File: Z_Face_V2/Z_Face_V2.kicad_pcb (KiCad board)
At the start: 4 copper layers, 100 x 100 mm, 24 parts, among them J1 CON-5040500591, J4 Conn_01x01, J5 Conn_01x01, J6 Conn_01x01, J7 Conn_01x01, U1 VEML7700, U2 DRV2605LDGS, U3 MCP9808_DFN

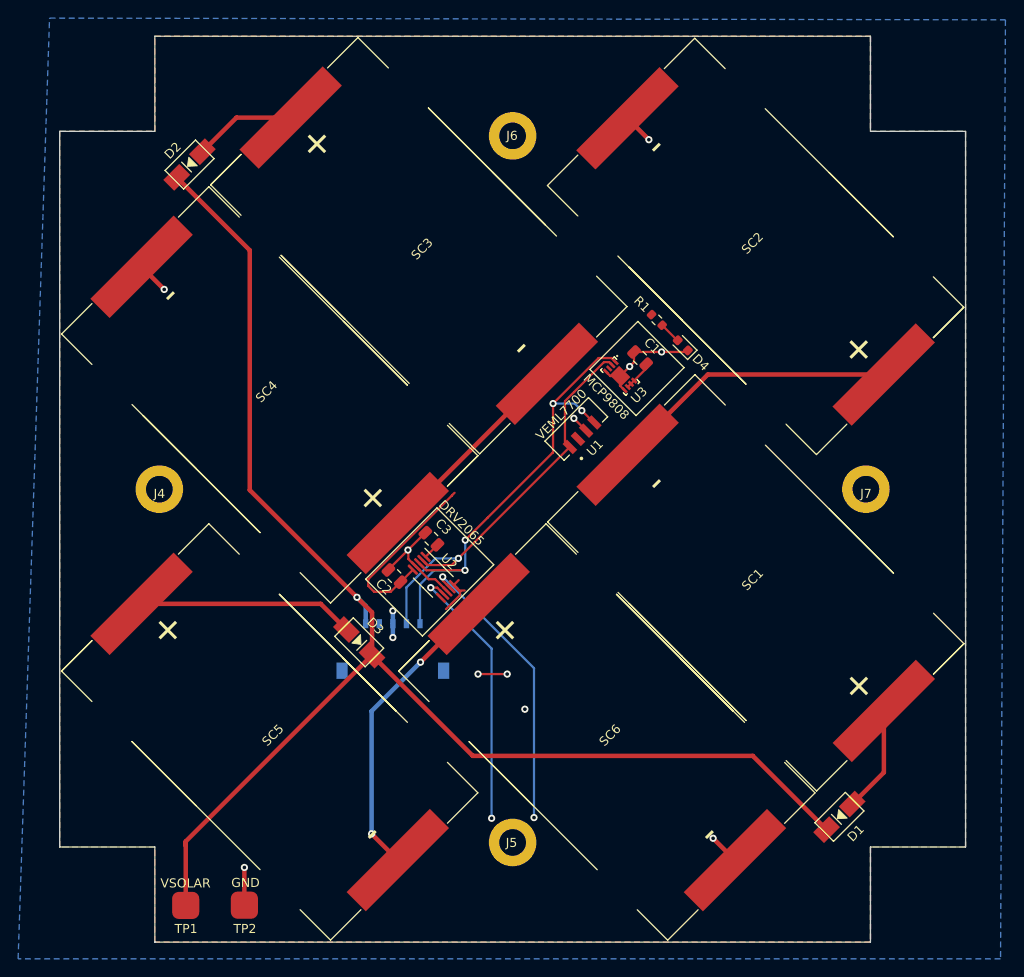
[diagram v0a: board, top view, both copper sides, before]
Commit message: Added 3-layer coil
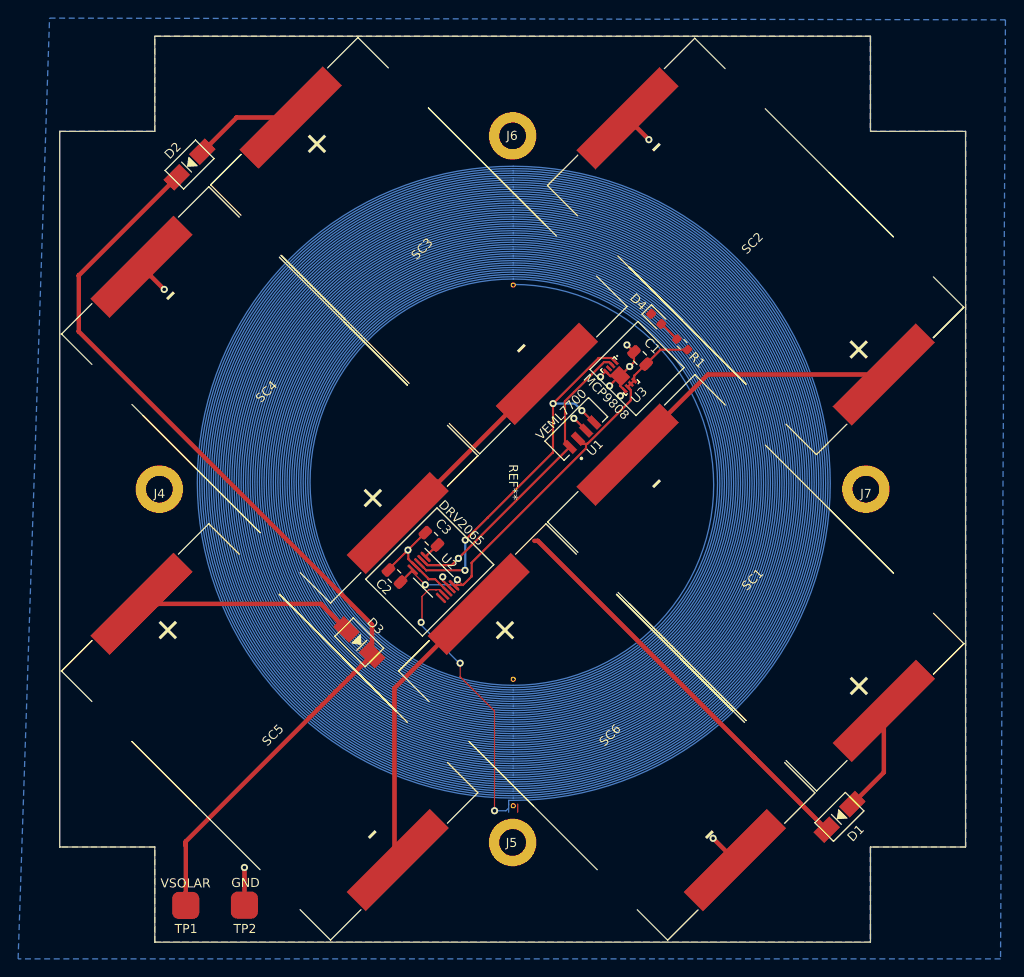
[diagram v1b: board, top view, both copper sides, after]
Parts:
- removed J1: CON-5040500591, SolarPanelBoards:CON_5040500591
- added REF**: 3Layer50Turn, dfsdf, F.Cu at (149.6, 84.2)
- moved D4 4.13 mm to (165.4, 66.2), turned to -45 degrees
- moved R1 3.89 mm to (168.2, 69.0), turned to 135 degrees
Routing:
- net Net-(U2-OUT+): track 10367.6 -> 47.9 mm, vias 5 -> 4
- net +3V3: track 32.6 -> 50.1 mm
- net SCL: track 44.8 -> 33.7 mm
- net SDA: track 52.3 -> 42.4 mm
- net VSOLAR: track 159.6 -> 152.9 mm, vias 1 -> 0
- net GND: track 45.0 -> 39.8 mm, vias 10 -> 11
- net Net-(SC5--): track 34.4 -> 32.3 mm, vias 2 -> 0
- added copper zone on F.Cu, net GND
- removed copper zone on F.Cu, net +3V3
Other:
- board text added: "PROVES BOTTOM CAP: V3 1U KIT"
- board text removed: "ADC I2C: JP1 Open (Defeult): 0x48 JP1 Solder Jumped: 0x49"
- board text removed: "ADC: ADS1015"
- board text removed: "C1 = 1uF C2 = 1uF C3 = 1uF"
- board text removed: "C4 = 1uF C5 = 0.01uF C6 = 0.01uF C7 = 0.1uF C8 = 10uF C9 = 10uF C10 = 0.1uF"
- board text removed: "CHEAT SHEET"
- board text removed: "Choose Your Favorite Size"
- board text removed: "Inside:"
- board text removed: "Outside:"
- board text removed: "PROVES BOTTOM CAP: YEARLING KIT"
- board text removed: "R1 = 1k-Ohm"
- board text removed: "R2 = 1M-Ohm R3 = 100-Ohm R4 = 100-Ohm R5 = 1k-Ohm R6 = 10k-Ohm"
- board text removed: "Thermocouple: AD8495"

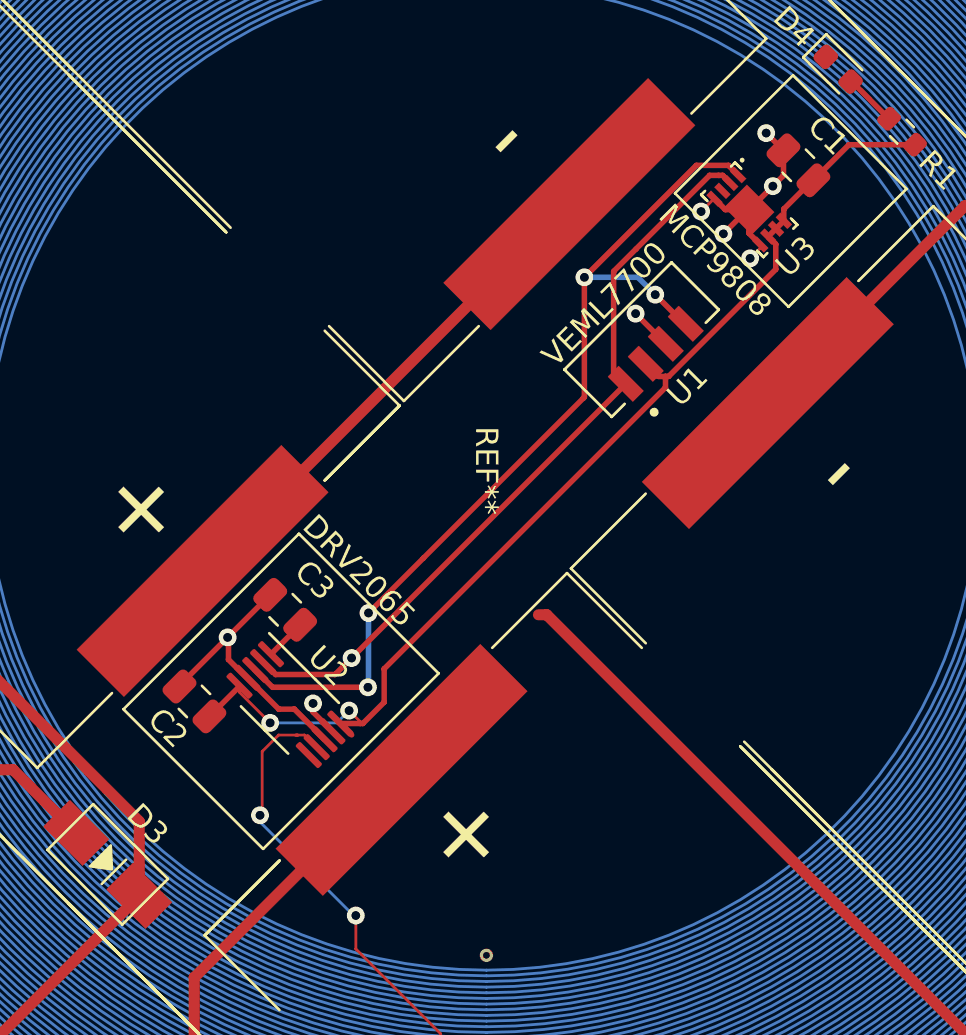
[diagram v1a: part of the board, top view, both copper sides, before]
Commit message: Updated Z- Layout Complete
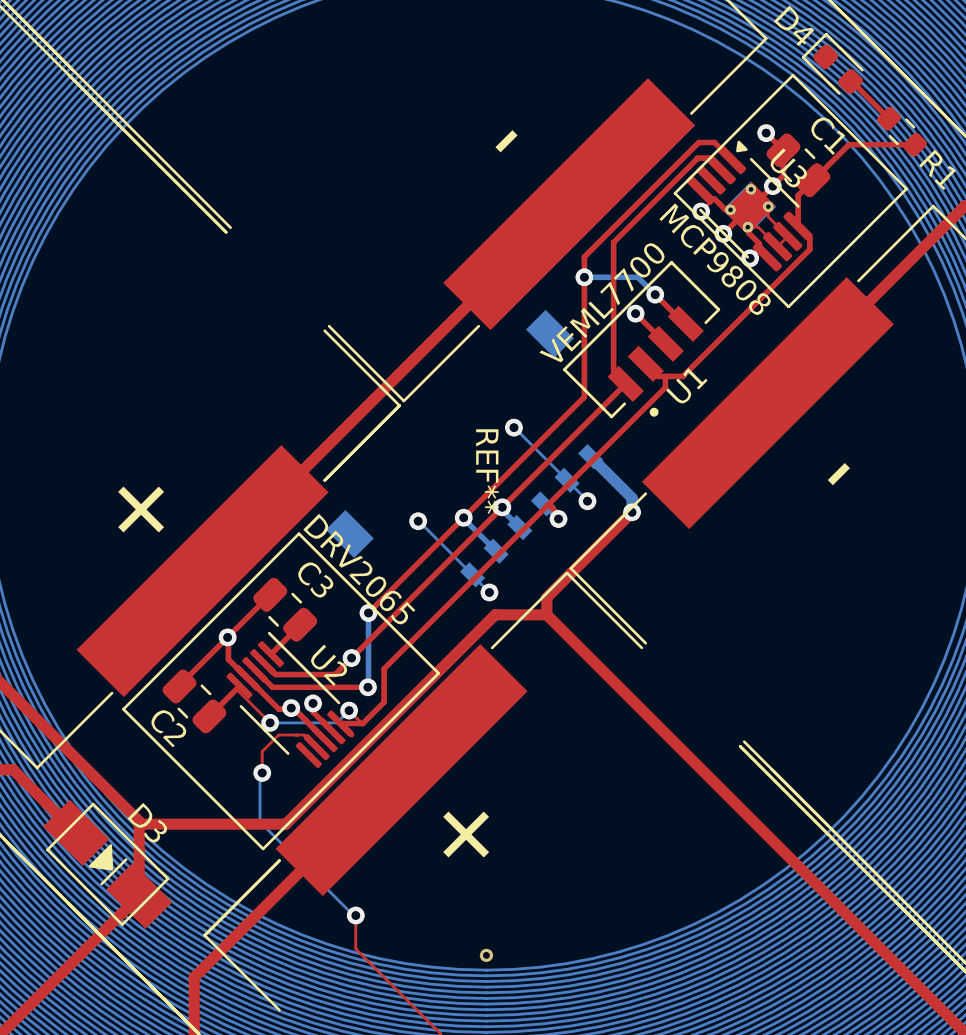
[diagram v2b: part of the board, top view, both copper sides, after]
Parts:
- added J1: FC Connection, Molex 6 pos:MOLEX_5040500691, B.Cu at (149.6, 84.2)
- U3: value MCP9808_DFN -> MCP9808T-E/MS; footprint SolarPanelBoards:MCP9808-NoLeadPackage -> Package_SO:MSOP-8-1EP_3x3mm_P0.65mm_EP1.5x1.8mm_ThermalVias
- moved U3 0.07 mm to (161.4, 72.5), turned to -45 degrees
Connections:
- U3 pad 3: unconnected-(U3-Alert-Pad3) -> (no net)
- U3 pad 6: +3V3 -> GND
- U3 pad 7: +3V3 -> GND
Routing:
- net VSOLAR: track 152.9 -> 184.2 mm, vias 0 -> 1
- net GND: track 39.8 -> 55.1 mm, vias 11 -> 16
- net SDA: track 42.4 -> 45.3 mm, vias 4 -> 5
- net +3V3: track 50.1 -> 52.5 mm, vias 2 -> 3
- net SCL: track 33.7 -> 35.7 mm, vias 1 -> 2
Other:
- board text added: "Original Design by Amanda Ewing V2 Update by Michael Pham"
- board text added: "Temp Sensor I2C Address 0x18"

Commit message: Completed V2 Z- Update
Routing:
- net GND: track 55.1 -> 61.3 mm, vias 16 -> 52
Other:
- board text added: "This board features a 50 turn 3 layer magnetorquer coil"

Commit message: Finished Design Tweaks for Z- V2
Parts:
- added G***: LOGO, LOGO, B.Cu at (126.5, 108.0)
- added G***: LOGO, LOGO, B.Cu at (173.0, 62.0)
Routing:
- net SCL: vias 2 -> 1
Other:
- board text added: "Original Design by Amanda Ewing V2 Update by Michael Pham C. March 2025"
- board text added: "This Board Was Brought to You By: Penguins Against Alzheimer's"
- board text removed: "Original Design by Amanda Ewing V2 Update by Michael Pham"
